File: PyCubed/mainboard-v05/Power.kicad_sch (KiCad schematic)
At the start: 82 parts, among them J14 Conn_01x06, Q1 IRLML2803, Q2 MBT2222ADW1T1, Q22 NDS8434, Q3 MBT2222ADW1T1, U17 BQ25883RGER, U21 TPS7A4501DCQT, U4 ADM1176-1ARMZ-R7, U5 TPS54226PWPRPWP14_2P31X2P46-L, U6 LTC4121

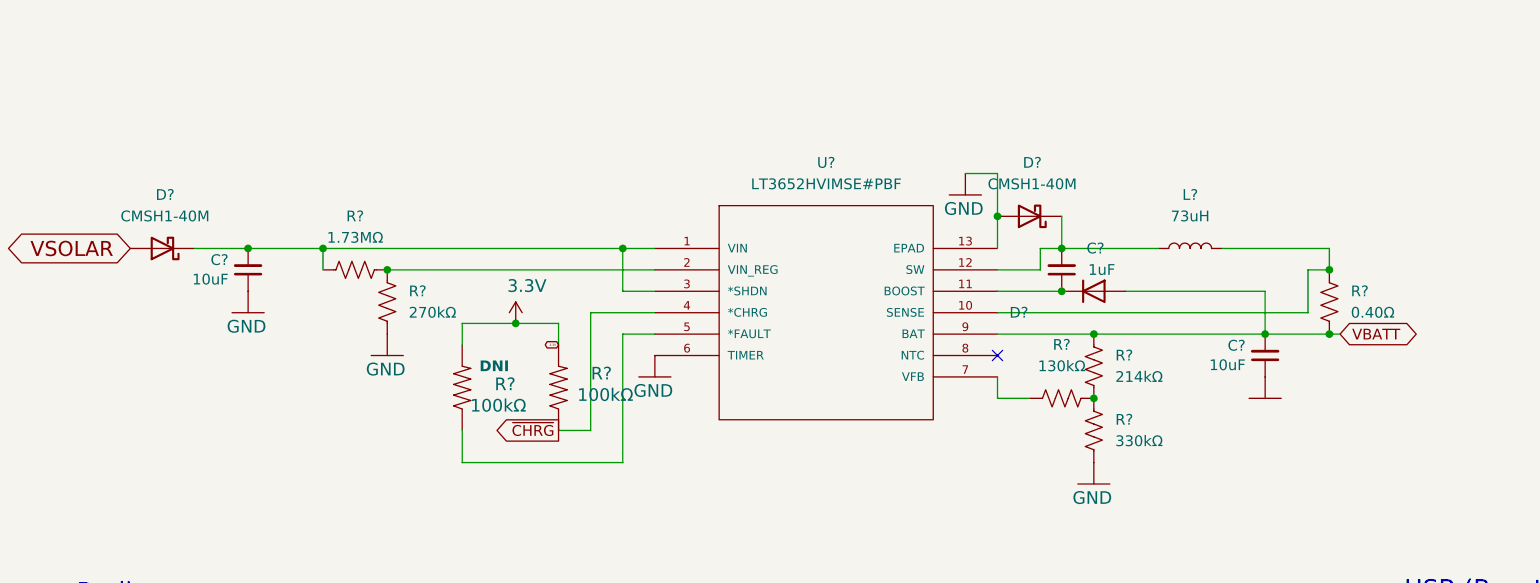
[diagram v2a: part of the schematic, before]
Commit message: add replacement sensors
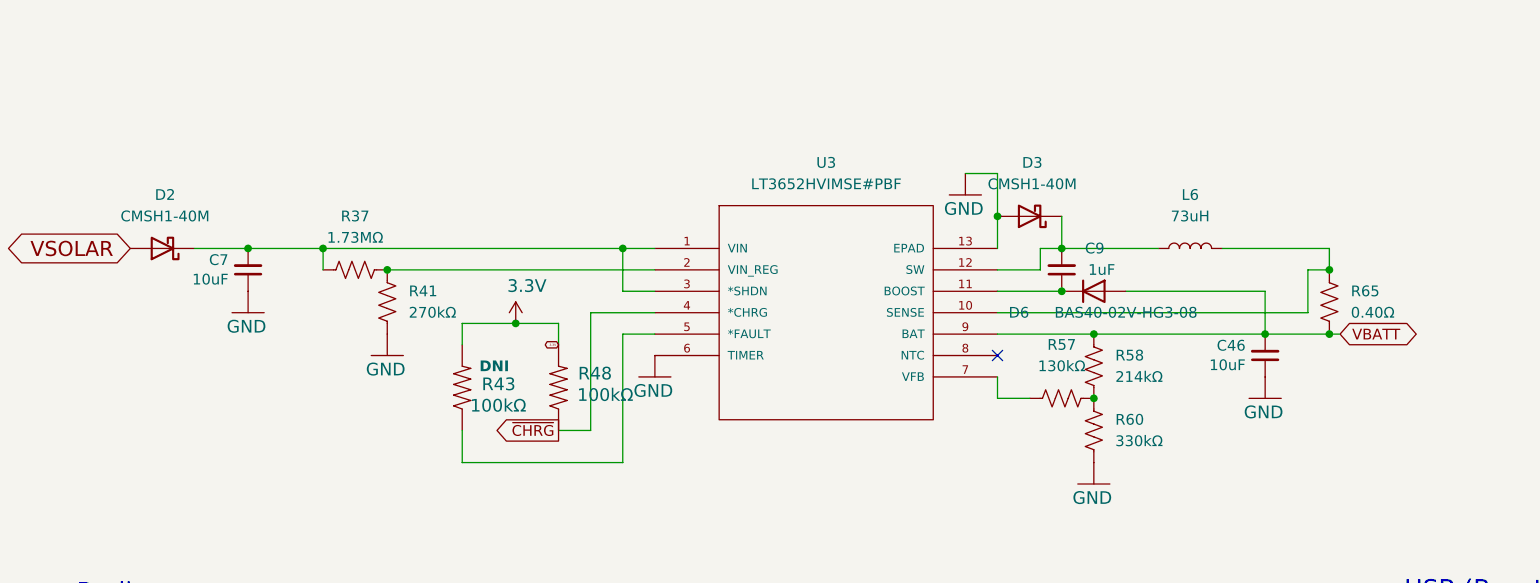
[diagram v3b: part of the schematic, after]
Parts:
- D6: renamed from D?; value (none) -> BAS40-02V-HG3-08
- gave numbers to parts that had none: 15
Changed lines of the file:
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@@
   )
   (text "Value is convenient,\nnot necessary. \n10K-80K would\nalso work for R29"
-    (at 129.54 140.97 0)
+    (at 129.54 140.97 180)
     (effects (font (size 0.7874 0.7874)) (justify right bottom))
   )
@@
   )
   (text "Add jumper to allow\nUSB to power the board\n(even inside P-Pod).\n"
-    (at 264.16 78.74 0)
+    (at 264.16 78.74 180)
     (effects (font (size 0.889 0.889)) (justify right bottom))
   )
@@
   (symbol (lib_id "mainboard:R-US_R0603") (at 67.31 54.61 90) (unit 1)
     (in_bom yes) (on_board yes)
-    (property "Reference" "R?" (id 0) (at 73.66 53.34 90)
+    (property "Reference" "R43" (id 0) (at 73.66 53.34 90)
       (effects (font (size 1.4986 1.4986)) (justify left bottom))
     )
@@
   (symbol (lib_id "Device:R_US") (at 138.43 55.88 90) (unit 1)
     (in_bom yes) (on_board yes) (fields_autoplaced)
-    (property "Reference" "R?" (id 0) (at 138.43 49.53 90))
+    (property "Reference" "R57" (id 0) (at 138.43 49.53 90))
     (property "Value" "130kΩ" (id 1) (at 138.43 52.07 90))
     (property "Footprint" "" (id 2) (at 138.684 54.864 90)
@@
   (symbol (lib_id "PycubedSymbols:LT3652HVIMSE#PBF") (at 59.69 38.1 0) (unit 1)
     (in_bom yes) (on_board yes) (fields_autoplaced)
-    (property "Reference" "U?" (id 0) (at 110.49 27.94 0))
+    (property "Reference" "U3" (id 0) (at 110.49 27.94 0))
     (property "Value" "LT3652HVIMSE#PBF" (id 1) (at 110.49 30.48 0))
     (property "Footprint" "MSOP-12_MSE" (id 2) (at 90.17 38.1 0)
@@
   (symbol (lib_id "mainboard:3.3V") (at 73.66 46.99 0) (unit 1)
     (in_bom yes) (on_board yes)
-    (property "Reference" "#P+?" (id 0) (at 73.66 46.99 0)
+    (property "Reference" "#P+0101" (id 0) (at 73.66 46.99 0)
       (effects (font (size 1.27 1.27)) hide)
     )
@@
   (symbol (lib_id "Device:R_US") (at 170.18 44.45 0) (unit 1)
     (in_bom yes) (on_board yes) (fields_autoplaced)
-    (property "Reference" "R?" (id 0) (at 172.72 43.1799 0)
+    (property "Reference" "R65" (id 0) (at 172.72 43.1799 0)
       (effects (font (size 1.27 1.27)) (justify left))
     )
@@
   (symbol (lib_id "Device:D_Schottky") (at 31.75 38.1 180) (unit 1)
     (in_bom yes) (on_board yes) (fields_autoplaced)
-    (property "Reference" "D?" (id 0) (at 32.0675 31.75 0))
+    (property "Reference" "D2" (id 0) (at 32.0675 31.75 0))
     (property "Value" "CMSH1-40M" (id 1) (at 32.0675 34.29 0))
     (property "Footprint" "" (id 2) (at 31.75 38.1 0)
@@
   (symbol (lib_id "Device:L") (at 153.67 38.1 90) (unit 1)
     (in_bom yes) (on_board yes) (fields_autoplaced)
-    (property "Reference" "L?" (id 0) (at 153.67 31.75 90))
+    (property "Reference" "L6" (id 0) (at 153.67 31.75 90))
     (property "Value" "73uH" (id 1) (at 153.67 34.29 90))
     (property "Footprint" "" (id 2) (at 153.67 38.1 0)
@@
   (symbol (lib_id "Device:R_US") (at 54.61 40.64 90) (unit 1)
     (in_bom yes) (on_board yes) (fields_autoplaced)
-    (property "Reference" "R?" (id 0) (at 54.61 34.29 90))
+    (property "Reference" "R37" (id 0) (at 54.61 34.29 90))
     (property "Value" "1.73MΩ" (id 1) (at 54.61 36.83 90))
     (property "Footprint" "" (id 2) (at 54.864 39.624 90)
@@
   (symbol (lib_id "mainboard:GND") (at 90.17 53.34 0) (unit 1)
     (in_bom yes) (on_board yes)
-    (property "Reference" "#GND?" (id 0) (at 90.17 53.34 0)
+    (property "Reference" "#GND0114" (id 0) (at 90.17 53.34 0)
       (effects (font (size 1.27 1.27)) hide)
     )
@@
   (symbol (lib_id "Device:C_Small") (at 41.91 40.64 180) (unit 1)
     (in_bom yes) (on_board yes)
-    (property "Reference" "C?" (id 0) (at 39.5986 39.4716 0)
+    (property "Reference" "C7" (id 0) (at 39.5986 39.4716 0)
       (effects (font (size 1.27 1.27)) (justify left))
     )
@@
   (symbol (lib_id "mainboard:GND") (at 41.91 45.72 0) (unit 1)
     (in_bom yes) (on_board yes)
-    (property "Reference" "#GND?" (id 0) (at 41.91 45.72 0)
+    (property "Reference" "#GND0123" (id 0) (at 41.91 45.72 0)
       (effects (font (size 1.27 1.27)) hide)
     )
@@
   (symbol (lib_id "mainboard:GND") (at 127 31.75 0) (unit 1)
     (in_bom yes) (on_board yes)
-    (property "Reference" "#GND?" (id 0) (at 127 31.75 0)
+    (property "Reference" "#GND0113" (id 0) (at 127 31.75 0)
       (effects (font (size 1.27 1.27)) hide)
     )
@@
   (symbol (lib_id "Device:R_US") (at 142.24 52.07 0) (unit 1)
     (in_bom yes) (on_board yes) (fields_autoplaced)
-    (property "Reference" "R?" (id 0) (at 144.78 50.7999 0)
+    (property "Reference" "R58" (id 0) (at 144.78 50.7999 0)
       (effects (font (size 1.27 1.27)) (justify left))
     )
@@
   (symbol (lib_id "mainboard:GND") (at 142.24 66.04 0) (unit 1)
     (in_bom yes) (on_board yes)
-    (property "Reference" "#GND?" (id 0) (at 142.24 66.04 0)
+    (property "Reference" "#GND0125" (id 0) (at 142.24 66.04 0)
       (effects (font (size 1.27 1.27)) hide)
     )
@@
   (symbol (lib_id "Device:C_Small") (at 138.43 40.64 180) (unit 1)
     (in_bom yes) (on_board yes)
-    (property "Reference" "C?" (id 0) (at 143.51 38.1 0)
+    (property "Reference" "C9" (id 0) (at 143.51 38.1 0)
       (effects (font (size 1.27 1.27)) (justify left))
     )
@@
   (symbol (lib_id "mainboard:GND") (at 58.42 50.8 0) (unit 1)
     (in_bom yes) (on_board yes)
-    (property "Reference" "#GND?" (id 0) (at 58.42 50.8 0)
+    (property "Reference" "#GND0112" (id 0) (at 58.42 50.8 0)
       (effects (font (size 1.27 1.27)) hide)
     )
@@
   (symbol (lib_id "Simulation_SPICE:DIODE") (at 142.24 43.18 180) (unit 1)
     (in_bom yes) (on_board yes)
-    (property "Reference" "D?" (id 0) (at 133.35 45.72 0))
-    (property "Value" "" (id 1) (at 146.05 45.72 0))
+    (property "Reference" "D6" (id 0) (at 133.35 45.72 0))
+    (property "Value" "BAS40-02V-HG3-08 " (id 1) (at 146.05 45.72 0))
     (property "Footprint" "" (id 2) (at 142.24 43.18 0)
       (effects (font (size 1.27 1.27)) hide)
@@
   (symbol (lib_id "Device:R_US") (at 142.24 59.69 0) (unit 1)
     (in_bom yes) (on_board yes) (fields_autoplaced)
-    (property "Reference" "R?" (id 0) (at 144.78 58.4199 0)
+    (property "Reference" "R60" (id 0) (at 144.78 58.4199 0)
       (effects (font (size 1.27 1.27)) (justify left))
     )
@@
   (symbol (lib_id "mainboard:GND") (at 162.56 55.88 0) (unit 1)
     (in_bom yes) (on_board yes)
-    (property "Reference" "#GND?" (id 0) (at 162.56 55.88 0)
-      (effects (font (size 1.27 1.27)) hide)
-    )
-    (property "Value" "" (id 1) (at 160.02 58.42 0)
+    (property "Reference" "#GND0124" (id 0) (at 162.56 55.88 0)
+      (effects (font (size 1.27 1.27)) hide)
+    )
+    (property "Value" "GND" (id 1) (at 160.02 58.42 0)
       (effects (font (size 1.4986 1.4986)) (justify left bottom))
     )
@@
   (symbol (lib_id "Device:C_Small") (at 162.56 50.8 180) (unit 1)
     (in_bom yes) (on_board yes)
-    (property "Reference" "C?" (id 0) (at 160.2486 49.6316 0)
+    (property "Reference" "C46" (id 0) (at 160.2486 49.6316 0)
       (effects (font (size 1.27 1.27)) (justify left))
     )
@@
   (symbol (lib_id "Device:R_US") (at 58.42 44.45 180) (unit 1)
     (in_bom yes) (on_board yes) (fields_autoplaced)
-    (property "Reference" "R?" (id 0) (at 60.96 43.1799 0)
+    (property "Reference" "R41" (id 0) (at 60.96 43.1799 0)
       (effects (font (size 1.27 1.27)) (justify right))
     )
@@
   (symbol (lib_id "mainboard:R-US_R0603") (at 78.74 54.61 90) (unit 1)
     (in_bom yes) (on_board yes)
-    (property "Reference" "R?" (id 0) (at 85.09 52.07 90)
+    (property "Reference" "R48" (id 0) (at 85.09 52.07 90)
       (effects (font (size 1.4986 1.4986)) (justify left bottom))
     )
@@
   (symbol (lib_id "Device:D_Schottky") (at 134.62 34.29 180) (unit 1)
     (in_bom yes) (on_board yes) (fields_autoplaced)
-    (property "Reference" "D?" (id 0) (at 134.9375 27.94 0))
+    (property "Reference" "D3" (id 0) (at 134.9375 27.94 0))
     (property "Value" "CMSH1-40M" (id 1) (at 134.9375 30.48 0))
     (property "Footprint" "" (id 2) (at 134.62 34.29 0)

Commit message: fixed vinreg
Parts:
- R37: value 1.73MΩ -> 183kΩ
- R41: value 270kΩ -> 27kΩ
- U3: footprint MSOP-12_MSE -> mainboard:MSOP-12_MSE
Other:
- note added: "Use 323kΩ for R37 and 20.5kΩ for R41 when LM234 is used."
- moved on the sheet: R37, R41
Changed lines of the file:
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@@
   (junction (at 49.53 127) (diameter 0) (color 0 0 0 0)
   )
+  (junction (at 48.26 38.1) (diameter 0) (color 0 0 0 0)
+  )
   (junction (at 46.99 176.53) (diameter 0) (color 0 0 0 0)
   )
@@
   (junction (at 148.59 -26.67) (diameter 0) (color 0 0 0 0)
   )
-  (junction (at 58.42 40.64) (diameter 0) (color 0 0 0 0)
+  (junction (at 57.15 40.64) (diameter 0) (color 0 0 0 0)
   )
   (junction (at 148.59 191.77) (diameter 0) (color 0 0 0 0)
@@
   (junction (at 162.56 48.26) (diameter 0) (color 0 0 0 0)
   )
-  (junction (at 50.8 38.1) (diameter 0) (color 0 0 0 0)
-  )
   (junction (at 204.47 138.43) (diameter 0) (color 0 0 0 0)
   )
@@
     (stroke (width 0) (type default) (color 0 0 0 0))
   )
-  (wire (pts (xy 50.8 38.1) (xy 50.8 40.64))
-    (stroke (width 0) (type default) (color 0 0 0 0))
-  )
   (wire (pts (xy 97.79 -34.29) (xy 97.79 -39.37))
     (stroke (width 0) (type default) (color 0 0 0 0))
@@
     (stroke (width 0) (type default) (color 0 0 0 0))
   )
+  (wire (pts (xy 48.26 38.1) (xy 86.36 38.1))
+    (stroke (width 0) (type default) (color 0 0 0 0))
+  )
   (wire (pts (xy 82.55 -21.59) (xy 82.55 -13.97))
     (stroke (width 0) (type default) (color 0 0 0 0))
@@
     (stroke (width 0) (type default) (color 0 0 0 0))
   )
-  (wire (pts (xy 50.8 38.1) (xy 86.36 38.1))
+  (wire (pts (xy 41.91 38.1) (xy 48.26 38.1))
     (stroke (width 0) (type default) (color 0 0 0 0))
   )
@@
     (stroke (width 0) (type default) (color 0 0 0 0))
   )
-  (wire (pts (xy 41.91 38.1) (xy 50.8 38.1))
-    (stroke (width 0) (type default) (color 0 0 0 0))
-  )
   (wire (pts (xy 30.48 105.41) (xy 44.45 105.41))
     (stroke (width 0) (type default) (color 0 0 0 0))
@@
     (stroke (width 0) (type default) (color 0 0 0 0))
   )
+  (wire (pts (xy 48.26 38.1) (xy 48.26 40.64))
+    (stroke (width 0) (type default) (color 0 0 0 0))
+  )
   (wire (pts (xy 138.43 -24.13) (xy 135.89 -24.13))
     (stroke (width 0) (type default) (color 0 0 0 0))
@@
     (stroke (width 0) (type default) (color 0 0 0 0))
   )
-  (wire (pts (xy 58.42 40.64) (xy 90.17 40.64))
+  (wire (pts (xy 57.15 40.64) (xy 90.17 40.64))
     (stroke (width 0) (type default) (color 0 0 0 0))
   )
@@
     (stroke (width 0) (type default) (color 0 0 0 0))
   )
+  (wire (pts (xy 57.15 41.91) (xy 57.15 40.64))
+    (stroke (width 0) (type default) (color 0 0 0 0))
+  )
   (wire (pts (xy 167.64 45.72) (xy 167.64 40.64))
     (stroke (width 0) (type default) (color 0 0 0 0))
@@
     (stroke (width 0) (type default) (color 0 0 0 0))
   )
+  (wire (pts (xy 55.88 40.64) (xy 57.15 40.64))
+    (stroke (width 0) (type default) (color 0 0 0 0))
+  )
   (wire (pts (xy 205.74 92.71) (xy 218.44 92.71))
     (stroke (width 0) (type default) (color 0 0 0 0))
@@
     (effects (font (size 1.0668 1.0668)) (justify left bottom))
   )
+  (text "Use 323kΩ for R37 \nand 20.5kΩ for R41 \nwhen LM234 is used."
+    (at 48.26 31.75 0)
+    (effects (font (size 1.27 1.27)) (justify left bottom))
+  )
   (text "RF Regulator" (at 62.23 87.63 0)
     (effects (font (size 2.159 2.159)) (justify left bottom))
@@
   )
   (text "Value is convenient,\nnot necessary. \n10K-80K would\nalso work for R29"
-    (at 129.54 140.97 180)
+    (at 129.54 140.97 0)
     (effects (font (size 0.7874 0.7874)) (justify right bottom))
   )
@@
   )
   (text "Add jumper to allow\nUSB to power the board\n(even inside P-Pod).\n"
-    (at 264.16 78.74 180)
+    (at 264.16 78.74 0)
     (effects (font (size 0.889 0.889)) (justify right bottom))
   )
@@
     (property "Reference" "U3" (id 0) (at 110.49 27.94 0))
     (property "Value" "LT3652HVIMSE#PBF" (id 1) (at 110.49 30.48 0))
-    (property "Footprint" "MSOP-12_MSE" (id 2) (at 90.17 38.1 0)
+    (property "Footprint" "mainboard:MSOP-12_MSE" (id 2) (at 90.17 38.1 0)
       (effects (font (size 1.27 1.27)) (justify bottom) hide)
     )
@@
     (pin "2")
   )
-  (symbol (lib_id "Device:R_US") (at 54.61 40.64 90) (unit 1)
+  (symbol (lib_id "Device:R_US") (at 52.07 40.64 90) (unit 1)
     (in_bom yes) (on_board yes) (fields_autoplaced)
-    (property "Reference" "R37" (id 0) (at 54.61 34.29 90))
-    (property "Value" "1.73MΩ" (id 1) (at 54.61 36.83 90))
-    (property "Footprint" "" (id 2) (at 54.864 39.624 90)
+    (property "Reference" "R37" (id 0) (at 52.07 34.29 90))
+    (property "Value" "183kΩ" (id 1) (at 52.07 36.83 90))
+    (property "Footprint" "" (id 2) (at 52.324 39.624 90)
       (effects (font (size 1.27 1.27)) hide)
     )
-    (property "Datasheet" "~" (id 3) (at 54.61 40.64 0)
+    (property "Datasheet" "~" (id 3) (at 52.07 40.64 0)
       (effects (font (size 1.27 1.27)) hide)
     )
@@
     (pin "2")
   )
-  (symbol (lib_id "mainboard:GND") (at 58.42 50.8 0) (unit 1)
+  (symbol (lib_id "mainboard:GND") (at 57.15 52.07 0) (unit 1)
     (in_bom yes) (on_board yes)
-    (property "Reference" "#GND0112" (id 0) (at 58.42 50.8 0)
+    (property "Reference" "#GND0112" (id 0) (at 57.15 52.07 0)
       (effects (font (size 1.27 1.27)) hide)
     )
-    (property "Value" "GND" (id 1) (at 55.88 53.34 0)
+    (property "Value" "GND" (id 1) (at 54.61 54.61 0)
       (effects (font (size 1.4986 1.4986)) (justify left bottom))
     )
-    (property "Footprint" "" (id 2) (at 58.42 50.8 0)
+    (property "Footprint" "" (id 2) (at 57.15 52.07 0)
       (effects (font (size 1.27 1.27)) hide)
     )
-    (property "Datasheet" "" (id 3) (at 58.42 50.8 0)
+    (property "Datasheet" "" (id 3) (at 57.15 52.07 0)
       (effects (font (size 1.27 1.27)) hide)
     )
@@
     (pin "2")
   )
-  (symbol (lib_id "Device:R_US") (at 58.42 44.45 180) (unit 1)
+  (symbol (lib_id "Device:R_US") (at 57.15 45.72 180) (unit 1)
     (in_bom yes) (on_board yes) (fields_autoplaced)
-    (property "Reference" "R41" (id 0) (at 60.96 43.1799 0)
+    (property "Reference" "R41" (id 0) (at 59.69 44.4499 0)
       (effects (font (size 1.27 1.27)) (justify right))
     )
-    (property "Value" "270kΩ" (id 1) (at 60.96 45.7199 0)
+    (property "Value" "27kΩ" (id 1) (at 59.69 46.9899 0)
       (effects (font (size 1.27 1.27)) (justify right))
     )
-    (property "Footprint" "" (id 2) (at 57.404 44.196 90)
+    (property "Footprint" "" (id 2) (at 56.134 45.466 90)
       (effects (font (size 1.27 1.27)) hide)
     )
-    (property "Datasheet" "~" (id 3) (at 58.42 44.45 0)
+    (property "Datasheet" "~" (id 3) (at 57.15 45.72 0)
       (effects (font (size 1.27 1.27)) hide)
     )

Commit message: fixed vreg stuff
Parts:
- R37: value 183kΩ -> 183MΩ
- U3: footprint mainboard:MSOP-12_MSE -> MSOP-12_MSE
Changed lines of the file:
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@@
     (property "Reference" "U3" (id 0) (at 110.49 27.94 0))
     (property "Value" "LT3652HVIMSE#PBF" (id 1) (at 110.49 30.48 0))
-    (property "Footprint" "mainboard:MSOP-12_MSE" (id 2) (at 90.17 38.1 0)
+    (property "Footprint" "MSOP-12_MSE" (id 2) (at 90.17 38.1 0)
       (effects (font (size 1.27 1.27)) (justify bottom) hide)
     )
@@
     (in_bom yes) (on_board yes) (fields_autoplaced)
     (property "Reference" "R37" (id 0) (at 52.07 34.29 90))
-    (property "Value" "183kΩ" (id 1) (at 52.07 36.83 90))
+    (property "Value" "183MΩ" (id 1) (at 52.07 36.83 90))
     (property "Footprint" "" (id 2) (at 52.324 39.624 90)
       (effects (font (size 1.27 1.27)) hide)

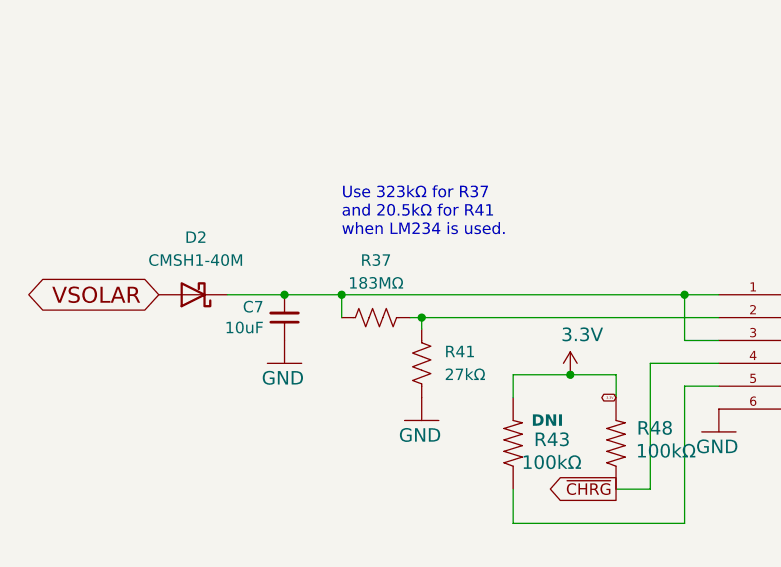
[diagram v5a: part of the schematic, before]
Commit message: Finished initial Power schematic
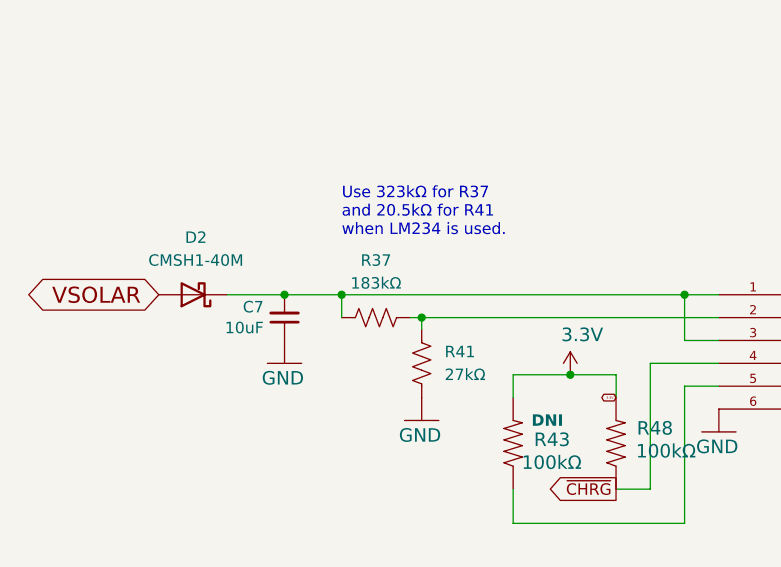
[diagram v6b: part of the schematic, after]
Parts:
- R37: value 183MΩ -> 183kΩ
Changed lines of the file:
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@@
     (in_bom yes) (on_board yes) (fields_autoplaced)
     (property "Reference" "R37" (id 0) (at 52.07 34.29 90))
-    (property "Value" "183MΩ" (id 1) (at 52.07 36.83 90))
+    (property "Value" "183kΩ" (id 1) (at 52.07 36.83 90))
     (property "Footprint" "" (id 2) (at 52.324 39.624 90)
       (effects (font (size 1.27 1.27)) hide)
